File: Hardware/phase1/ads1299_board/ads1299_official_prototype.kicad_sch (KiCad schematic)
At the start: 103 parts, among them J1 Conn_02x05_Odd_Even, J6 36PIN_IDC, U1 ADS1299IPAG, U11 OPA376, U2 NI, U3 132134, U4 OPA376

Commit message: ads1299 PCB update (1.22.25)
- left off on figuring out all the "Not Installed" footprints
- some components may have the wrong designator
- some components are missing footprints
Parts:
- added R14: 0, RC0402JR-070RL:RESC1005X40, symbol Device:R_Small
- AIN1: renamed from U3; value 132134 -> AIN1; footprint 132134_AMP -> 132134:132134_AMP
- C1, C11, C17, C2, C23, C24, C3, C4, C5, C6, C76, C77, C99: footprint (none) -> GRM188R61E105KA12D:CAPC1608X90N
- C10: footprint (none) -> GRM219R61A106KE44D:CAPC2012X95N
- C12, C13, C14, C16, C18, C95: footprint (none) -> GRM188R71H104KA93D:CAPC1608X90N
- C20: footprint (none) -> GRM188R71H103KA01D:CAPC1608X90N
- C72: renamed from C94; footprint (none) -> GRM188R71H472KA01D:CAPC1608X90N
- C73: renamed from C95; footprint (none) -> GRM188R71H472KA01D:CAPC1608X90N
- C75, C80, C81, C82, C83, C84, C85, C86, C87, C88, C89, C90, C91, C92, C93: footprint (none) -> GRM188R71H472KA01D:CAPC1608X90N
- C9: footprint (none) -> LMK325BJ107MM_T:CAPC3225X280N
- C97: renamed from C23; footprint (none) -> GRM188R61E105KA12D:CAPC1608X90N
- C98: renamed from C26; value 0.1uF -> NI
- J5: renamed from J1; value Conn_02x05_Odd_Even -> NI
- JP5: value NI -> TSW-102-07-T-S
- OSC1: footprint FXO-HC735-8:XTAL_FXO-HC735-8 -> FXO-HC735:XTAL_FXO-HC735-8
- R10, R11, R12, R80, R81, R82, R83, R84, R85, R86, R87, R88, R89, R90, R91, R92, R93, R94, R95: footprint (none) -> RC0603FR-074K99L:RESC1608X60N
- R13, R15: footprint (none) -> RC0402JR-070RL:RESC1005X40
- R23: renamed from R1; footprint (none) -> RC0603JR-072ML:0603
- R24: footprint (none) -> RC0603JR-072ML:0603
- R25, R3: footprint (none) -> RC0603JR-070RL:RESC1607X60N
- R6, R7, R75: footprint (none) -> RC0603FR-0710KL:RESC1607X60N
- R8: footprint (none) -> RC0603FR-07392KL:RESC1608X55N
- U1: footprint PAG64_TEX -> ADS1299CPAG:QFP64P50_1200X1200X120L60X22N
- U2: footprint Package_TO_SOT_SMD:SOT-23-5 -> (none)
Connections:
- net AVDD: no longer C12.1, C5.1
- net DVDD: now also C12.1, C5.1
- net at U4.2 (-IN), U4.6 (OUT): now also R14.2; no longer JP8.01
- new net: JP8.01, R14.1

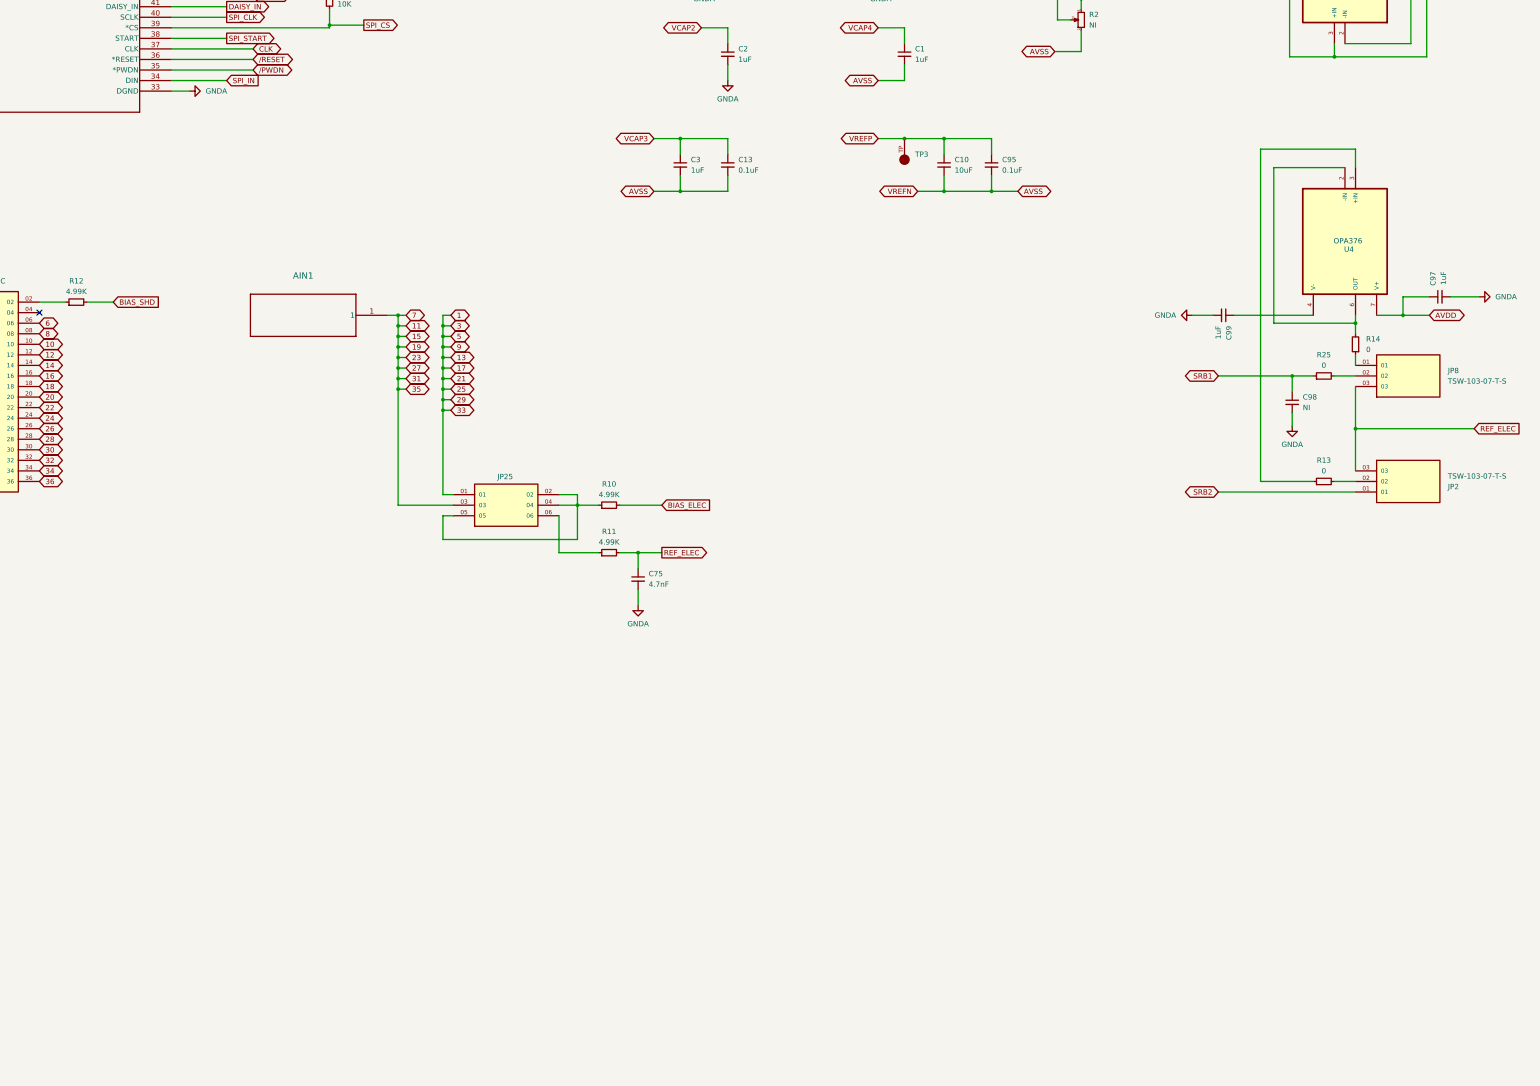
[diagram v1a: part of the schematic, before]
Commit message: ads1299 update (1.30.25)
- omit all NI components
- i still think it is a good idea to expose all pins for now, so i left off on implementing "Figure 62. ECG MDK Board Interface Adapter"
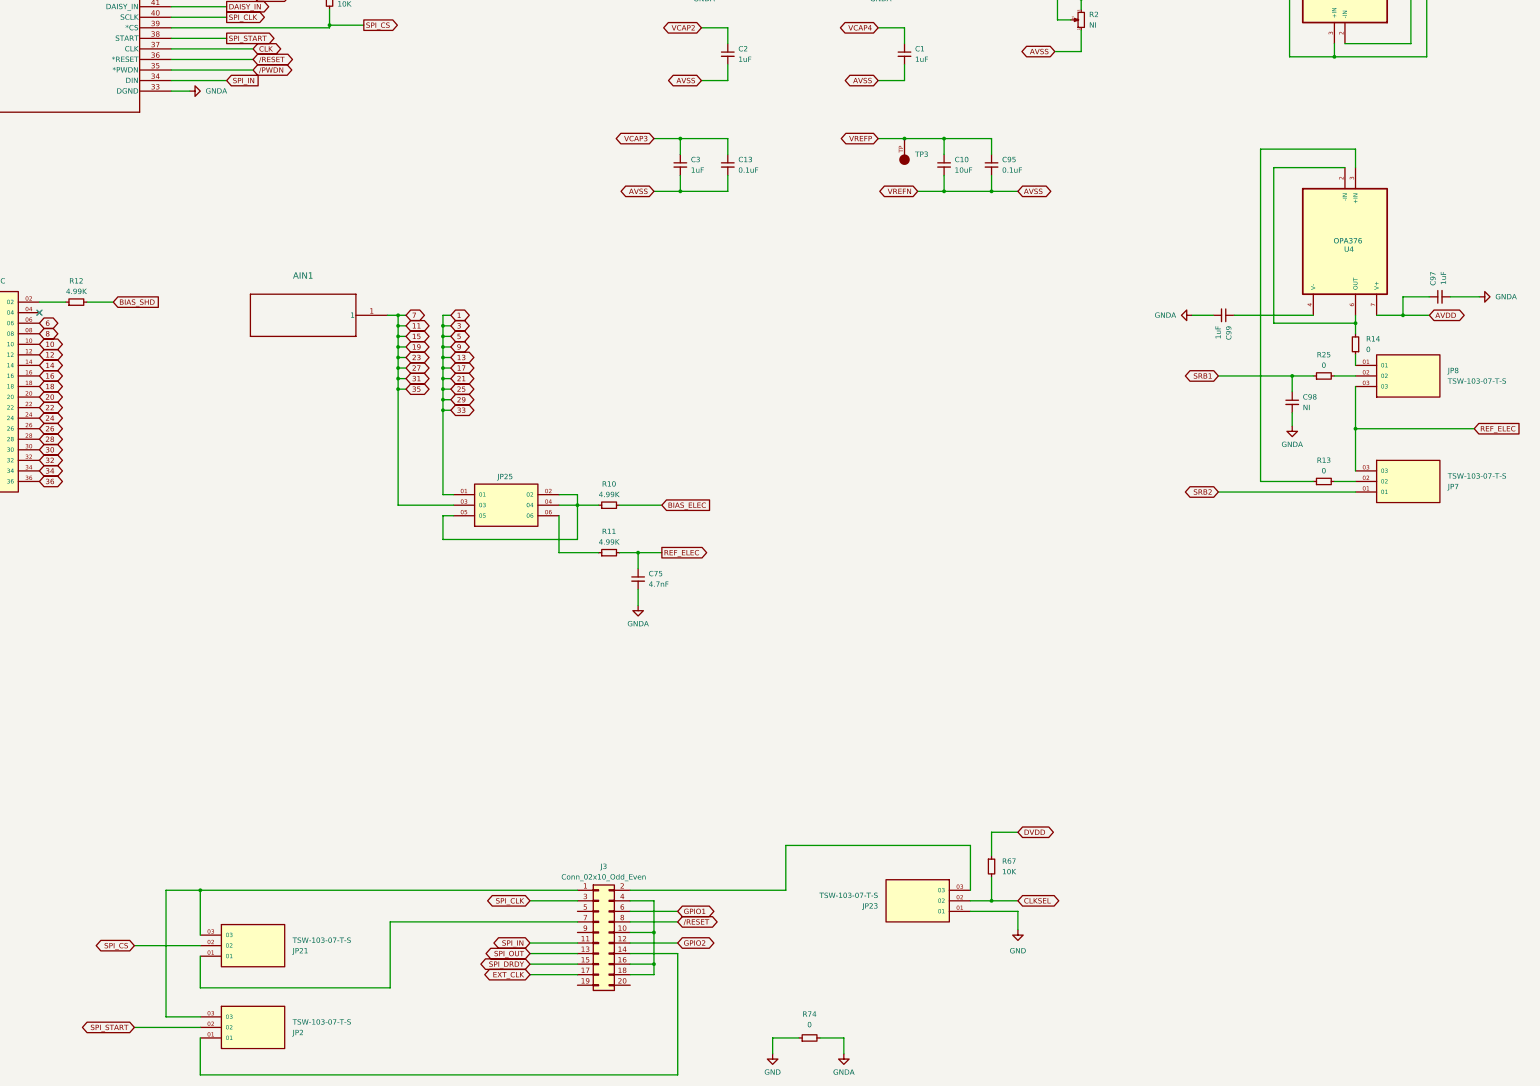
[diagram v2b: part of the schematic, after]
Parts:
- added J3: Conn_02x10_Odd_Even, symbol Connector_Generic:Conn_02x10_Odd_Even
- added JP2, JP21, JP23: TSW-103-07-T-S, TSW-103-07-T-S:SAMTEC_TSW-103-07-T-S, symbol TSW-103-07-T-S:TSW-103-07-T-S
- added R67: 10K, symbol Device:R_Small
- added R74: 0, symbol Device:R_Small
- renumbered JP2 to JP7
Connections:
- net AVSS: now also C2.2
- net CLKSEL: now also JP23.02, R67.2
- net DVDD: now also R67.1
- net EXT_CLK: now also J3.17 (Pin_17)
- net GNDA: now also R74.2; no longer C2.2
- net GPIO1: now also J3.6 (Pin_6)
- net GPIO2: now also J3.12 (Pin_12)
- net SPI_CLK: now also J3.3 (Pin_3)
- net SPI_CS: now also JP21.02
- net SPI_DRDY: now also J3.15 (Pin_15)
- net SPI_IN: now also J3.11 (Pin_11)
- net SPI_OUT: now also J3.13 (Pin_13)
- net SPI_START: now also JP2.02
- net /RESET: now also J3.8 (Pin_8)
- new net: J3.2 (Pin_2), JP23.03
- new net: J3.14 (Pin_14), JP2.01
- new net: J3.1 (Pin_1), JP2.03, JP21.03
- new net: J3.7 (Pin_7), JP21.01
- new net: J3.10 (Pin_10), J3.16 (Pin_16), J3.18 (Pin_18), J3.4 (Pin_4)
- new net GND: JP23.01, R74.1

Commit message: first update of the day (2.5.25)
- footprints need to be verified
- layout needs to be optimized
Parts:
- added C68, C71: 100uF, LMK325BJ107MM_T:CAPC3225X280N, symbol Device:C_Small
- added C69, C70, C94: 0.1uF, GRM188R71H104KA93D:CAPC1608X90N, symbol Device:C_Small
- added J4: ~, SSW-105-22-F-D-VS-K:SAMTEC_SSW-105-22-F-D-VS-K, symbol Connector_Generic:Conn_02x05_Odd_Even
- added JP24: TSW-103-07-T-S, TSW-103-07-T-S:SAMTEC_TSW-103-07-T-S, symbol TSW-103-07-T-S:TSW-103-07-T-S
- added JP4: TSW-102-07-T-S, TSW-102-07-T-S:SAMTEC_TSW-102-07-T-S, symbol TSW-102-07-T-S:TSW-102-07-T-S
- added R71, R72, R73: 0, RC0402JR-070RL:RESC1005X40, symbol Device:R_Small
- added TP10, TP7, TP8, TP9: 5001, 5001:KEYSTONE_5001, symbol 5001:5001
- added U10: 24AA256-I/ST, 24AA256-I_ST:SOP8P65_300X640X120L60X24N, symbol Connector_Generic:Conn_02x04_Counter_Clockwise
- J3: footprint (none) -> TSM-110-01-T-DV-P-TR:SAMTEC_TSM-110-01-T-DV-P-TR
- R67: footprint (none) -> RC0603FR-0710KL:RESC1607X60N
- R74: footprint (none) -> RC0402JR-070RL:RESC1005X40
- renumbered JP2 to JP22
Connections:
- net DVDD: now also C70.1, C71.1, JP24.02
- net GND: now also C68.2, C69.2, C94.2, J4.5 (Pin_5), R71.1, R72.1, R73.1, TP8.TP, U10.4 (Pin_4), U10.7 (Pin_7)
- net GNDA: now also J3.10 (Pin_10), J3.18 (Pin_18), J3.4 (Pin_4), C70.2, C71.2
- net SDA: now reaches J3.20 (Pin_20)
- net SDA: now also U10.5 (Pin_5)
- new net: J4.10 (Pin_10), JP4.02
- new net: J4.9 (Pin_9), JP24.01, TP10.TP
- new net: J4.7 (Pin_7), JP24.03, TP9.TP
- new net +3V3: C94.1, R71.2, R72.2, R73.2, U10.1 (Pin_1), U10.2 (Pin_2), U10.3 (Pin_3), U10.8 (Pin_8)
- new net +5V: C68.1, C69.1, JP4.01, TP7.TP
- new net SCL: J3.16 (Pin_16), U10.6 (Pin_6)
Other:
- moved on the sheet: R74

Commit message: ads1299 2nd update (2.5.25)
- verified footprints
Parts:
- removed C20: 0.01uF, GRM188R71H103KA01D:CAPC1608X90N, symbol Device:C_Small
- removed C21, C22, C33: NI, symbol Device:C_Small
- removed C23, C24: 1uF, GRM188R61E105KA12D:CAPC1608X90N, symbol Device:C_Small
- removed JP1, JP6: TSW-103-07-T-S, TSW-103-07-T-S:SAMTEC_TSW-103-07-T-S, symbol TSW-103-07-T-S:TSW-103-07-T-S
- removed JP17: TSW-102-07-T-S, TSW-102-07-T-S:SAMTEC_TSW-102-07-T-S, symbol TSW-102-07-T-S:TSW-102-07-T-S
- removed R1, R4, R5: NI, symbol Device:R_Small
- removed R15: 0, RC0402JR-070RL:RESC1005X40, symbol Device:R_Small
- removed R2: NI, symbol Device:R_Potentiometer_Small
- removed R23, R24: 2M, RC0603JR-072ML:0603, symbol Device:R_Small
- removed R3: 0, RC0603JR-070RL:RESC1607X60N, symbol Device:R_Small
- removed R8: 392K, RC0603FR-07392KL:RESC1608X55N, symbol Device:R_Small
- removed U11: OPA376, OPA376AID:SOIC127P599X175-8N, symbol OPA376AID:OPA376AID
- removed U2: NI, symbol Amplifier_Operational:OPA842xDBV
- added C25: 1uF, GRM188R61E105KA12D:CAPC1608X90N, symbol Device:C_Small
- added C26: 0.1uF, GRM188R71H104KA93D:CAPC1608X90N, symbol Device:C_Small
- C15, C19: value NI -> 0.1uF; footprint (none) -> GRM188R71H104KA93D:CAPC1608X90N
- C7, C8: value NI -> 1uF; footprint (none) -> GRM188R61E105KA12D:CAPC1608X90N
- C98: value NI -> 0.01uF; footprint (none) -> GRM188R71H104KA93D:CAPC1608X90N
- J5: value NI -> ~; footprint (none) -> SSW-105-22-F-D-VS-K:SAMTEC_SSW-105-22-F-D-VS-K
- TP10, TP7, TP9: footprint 5001:KEYSTONE_5001 -> 5000:KEYSTONE_5000
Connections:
- net AVDD: now also C25.1, C26.1
- net AVSS: now also C9.2
- net GNDA: now also C25.2, C26.2; no longer C9.2
- net BIASIN: no longer names the net of U1.62 (BIASIN)
- net BIASINV: no longer names the net of U1.61 (BIASINV)
- net BIASOUT: no longer names the net of U1.63 (BIASOUT)
- net BIASREF: no longer names the net of U1.60 (BIASREF)
- no-connect marks 3 -> 7
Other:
- moved on the sheet: C1, C10, C12, C13, C14, C15, C16, C17, C18, C19, C2, C3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

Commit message: ads1299 board 3rd update of today (2.5.25)
- still need to finish implementing barreljack and ECG power supply circuitry (both schematic/layout)
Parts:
- removed C25: 1uF, GRM188R61E105KA12D:CAPC1608X90N, symbol Device:C_Small
- removed C26: 0.1uF, GRM188R71H104KA93D:CAPC1608X90N, symbol Device:C_Small
- added 10_C1, 10_C3: 0.1uF, GRM188R71H104KA93D:CAPC1608X90N, symbol Device:C_Small
- added 10_C2: 0.01uF, GRM188R71H103KA01D:CAPC1608X90N, symbol Device:C_Small
- added 10_C4: 10uF, GRM219R61A106KE44D:CAPC2012X95N, symbol Device:C_Small
- added 10_C40, 10_C41: 68uF, symbol Device:C_Polarized_Small
- added 10_J12: TSW-102-07-T-S, TSW-102-07-T-S:SAMTEC_TSW-102-07-T-S, symbol TSW-102-07-T-S:TSW-102-07-T-S
- added 10_J2: PJ-102B, PJ-102B:CUI_PJ-102B, symbol PJ-102B:PJ-102B
- added 10_R14: 9.31K, RC0603FR-079K31L:RC0603N_YAG, symbol Device:R_Small
- added 10_R15: 51.1K, RC0603FR_0751K1L:RC0603N_YAG, symbol Device:R_Small
- added 10_R16, 10_R17: 30.1K, RC0603FR-0730K1L:RC0603N_YAG, symbol Device:R_Small
- added 10_R2: 10K, RC0603FR-0710KL:RESC1607X60N, symbol Device:R_Small
- added 10_S3: RESET, symbol Switch:SW_Push
- added U2: REG104GA-5, REG104GA-5:SOT127P706X180-6N, symbol REG104GA-5:REG104GA-5
- added U3: TPS70302PWP, TPS70302PWP:SOP65P640X120-25N, symbol TPS70302PWP:TPS70302PWP
- C98: footprint GRM188R71H104KA93D:CAPC1608X90N -> GRM188R71H103KA01D:CAPC1608X90N
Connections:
- net BIAS_ELEC is gone; now on net GNDA: R10.2
- net +3V3: now also 10_C41.1, 10_R15.1, 10_R2.1, U3.22 (VOUT1_2), U3.23 (VOUT1), U3.5 (~MR2)
- net +5V: now also 10_C3.1, 10_C4.1, 10_J12.01, U3.10 (VIN2_2), U3.11 (VIN2), U3.2 (VIN1_2), U3.3 (VIN1), U3.8 (SEQ)
- net GND: now also 10_C1.2, 10_C2.2, 10_C3.2, 10_C4.2, 10_C40.2, 10_C41.2, 10_J2.3, 10_R16.2, 10_R17.2, 10_S3.2, U2.3 (GND), U3.1 (GND/HEATSINK_4), U3.12 (GND/HEATSINK_2), U3.13 (GND/HEATSINK_3), U3.24 (GND/HEATSINK), U3.7 (~EN), U3.9 (GND)
- net SRB1: no longer U1.17 (SRB1)
- net SRB2: no longer U1.18 (SRB2)
- new net: 10_J12.02, U2.2 (VOUT)
- new net: 10_C1.1, 10_J2.1, U2.1 (VIN), U2.5 (ENABLE)
- new net: 10_C2.1, U2.4 (NR/ADJUST)
- new net +1V5: 10_C40.1, 10_R14.1, U3.14 (VOUT2_2), U3.15 (VOUT2)
- new net FB1: 10_R15.2, 10_R17.1, U3.21 (V_SENSE1_/_FB1)
- new net FB2: 10_R14.2, 10_R16.1, U3.16 (V_SENSE2_/_FB2)
- new net /MR1: 10_R2.2, 10_S3.1, U3.6 (~MR1)
- no-connect marks 7 -> 11

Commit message: barrel jack update ads1299 (2.8.25)
- schematic seems to be done
- might have some power flag issues
- many components require footprint assignments still, base those footprints off the ADS1299 BOM
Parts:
- added 10_C25, C45, C46, C50, C51, C60, C61, C65, C66: 10uF, symbol Device:C_Small
- added 10_C30, 10_C38: 68uF, symbol Device:C_Polarized_Small
- added 10_C31, C59, C63, C64: 2.2uF, symbol Device:C_Small
- added 10_C9, C67: 0.01uF, symbol Device:C_Small
- added 10_J13A, 10_J13B: Conn_01x02, symbol Connector_Generic:Conn_01x02
- added 10_J14: Screw_Terminal_01x06, symbol Connector:Screw_Terminal_01x06
- added 10_J9: AMPPWR, symbol Connector_Generic:Conn_02x03_Odd_Even
- added 10_U7: TPS79618DCQ, TPS79618DCQ:SOT127P706X180-6N, symbol PH_TPS79618DCQ:TS5205CX525_RFG
- added C47, C48, C49, C58, C62: 1uF, symbol Device:C_Small
- added C57: 0.1uF, symbol Device:C_Small
- added J1: Conn_02x05_Odd_Even, symbol Connector_Generic:Conn_02x05_Odd_Even
- added JP2, JP20: Conn_01x03, symbol Connector_Generic:Conn_01x03
- added L1, L2, L3, L4, L5: 3.3uH, MLZ2012A3R3W:INDC2012X87N, symbol MLZ2012A3R3W:MLZ2012A3R3W
- added TP13, TP4, TP5, TP6: 5001, 5001:KEYSTONE_5001, symbol 5001:5001
- added U5: TPS60403DBVT, TPS60403DBVT:SOT95P280X145-5N, symbol TPS60403DBVT:TPS60403DBVT
- added U6: TPS73225DBVT, TPS73225DBVT:SOT95P280X145-5N, symbol TPS73225DBVT:TPS73225DBVT
- added U7: TPS72325DBVT, TPS72325DBVT:SOT95P280X145-5N, symbol TPS72325DBVT:TPS72325DBVT
- 10_J2: footprint PJ-102B:CUI_PJ-102B -> PJ_102B:CUI_PJ-102B
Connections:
- net +3V3: now also J4.9 (Pin_9), JP24.01, TP10.TP, J1.9 (Pin_9)
- net +5V: now also 10_C31.1, 10_J13A.2 (Pin_2), 10_J13B.2 (Pin_2), 10_J14.5 (Pin_5), 10_U7.1 (EN), 10_U7.2 (IN), C45.1, C46.1, C47.1, C58.1, J1.10 (Pin_10), JP2.3 (Pin_3), L1.1, L1.2, TP5.TP, U5.2 (IN), U6.1 (IN), U6.3 (EN)
- net AVDD: now also C57.1, JP2.2 (Pin_2)
- net AVSS: now also C57.2, JP20.2 (Pin_2)
- net GNDA: now also 10_C25.2, 10_C30.2, 10_C31.2, 10_C38.2, 10_C9.2, 10_J14.6 (Pin_6), 10_J9.5 (Pin_5), 10_J9.6 (Pin_6), 10_U7.3 (GND), C45.2, C46.2, C47.2, C49.2, C50.2, C51.2, C58.2, C59.2, C60.2, C61.2, C62.2, C63.2, C64.2, C65.2, C66.2, C67.2, J1.5 (Pin_5), J1.6 (Pin_6), JP20.3 (Pin_3), U6.2 (GND), U7.1 (GND)
- net +1V8: now reaches J4.7 (Pin_7), JP24.03, TP9.TP
- net +1V8: now also 10_C25.1, 10_U7.4 (OUT), J1.7 (Pin_7)
- net +1V5 renamed +1V6
- new net: C49.1, C50.1, L2.1, U5.1 (OUT)
- new net: C59.1, C60.1, L5.1, U6.5 (OUT)
- new net: C61.1, JP2.1 (Pin_1), L5.2, TP13.TP
- new net: C64.1, C65.1, L4.1, U7.5 (OUT)
- new net: C62.1, U6.4 (NR)
- new net: C66.1, JP20.1 (Pin_1), L4.2, TP6.TP
- new net: C48.2, U5.3 (CFLY-)
- new net: C48.1, U5.5 (CFLY+)
- new net: 10_C9.1, 10_U7.5 (BYP/FB)
- new net: C67.1, U7.4 (NR)
- new net +5VA: 10_C30.1, 10_C38.1, 10_J13B.1 (Pin_1), 10_J14.3 (Pin_3), 10_J9.3 (Pin_3), J1.3 (Pin_3)
- new net +VA: 10_J13A.1 (Pin_1), 10_J14.2 (Pin_2), 10_J9.1 (Pin_1), J1.1 (Pin_1)
- new net -5V: C51.1, C63.1, L2.2, TP4.TP, U7.2 (IN), U7.3 (EN)
- new net -5VA: 10_J14.4 (Pin_4), 10_J9.4 (Pin_4), J1.4 (Pin_4)
- new net -VA: 10_J14.1 (Pin_1), 10_J9.2 (Pin_2), J1.2 (Pin_2)
- no-connect marks 11 -> 12
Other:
- moved on the sheet: 10_C1, 10_C2, 10_C3, 10_C4, 10_C40, 10_C41, 10_J12, 10_J2, 10_R14, 10_R15, 10_R16, 10_R17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
